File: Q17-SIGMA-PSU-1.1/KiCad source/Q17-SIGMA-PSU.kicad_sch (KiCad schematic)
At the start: 80 parts, among them J1-1 V+ (IN), J1-2 GND, J1-3 V- (IN), J2-1 V+, J2-2 V+, J2-3 GND, J2-4 GND, J2-5 GND, J2-6 V-, J2-7 V-, Q1 BC548B, Q2 BC558B, Q3 BC548B, Q4 BC556B, Q5 BC546B, Q6 IRFZ24NPBF, Q7 IRF9Z34NPBF, Q8 IRFZ24NPBF, Q9 IRF9Z34NPBF, U1 ZHB6792TA, U2 ZHB6792TA

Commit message: Update diagram
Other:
- note added: "Q6, Q8 : IRFZ24NPBF, IRFZ34NPBF or IRF530NPBF"
- note removed: "Q6, Q8 : IRFZ24NPBF or IRF530NPBF"
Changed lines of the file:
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@@
 	(title_block
 		(title "Q17-SIGMA Power Supply")
-		(date "2024-04-30")
-		(rev "1.1.1")
+		(date "2024-05-04")
+		(rev "1.1.2")
 		(company "PCB and BOM by stef")
 		(comment 2 "Design and test by Moor")
@@
 		)
 	)
-	(text "Q6, Q8 : IRFZ24NPBF or IRF530NPBF"
+	(text "Q6, Q8 : IRFZ24NPBF, IRFZ34NPBF or IRF530NPBF"
 		(exclude_from_sim no)
 		(at 14.478 150.622 0)

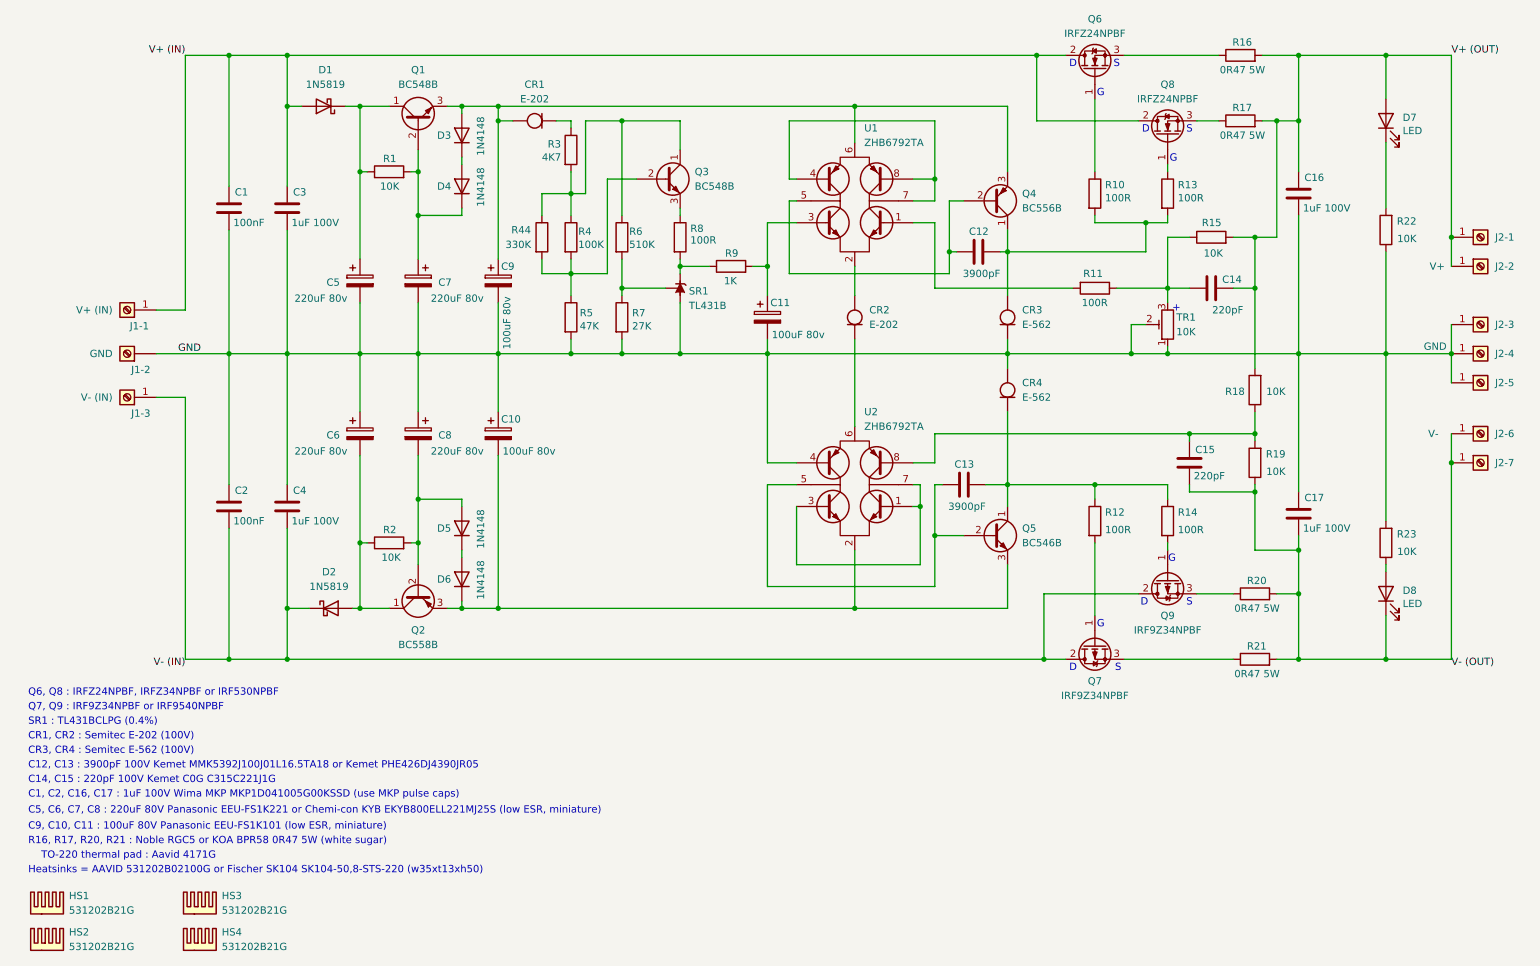
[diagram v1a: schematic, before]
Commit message: Update sigma diagram with real measures
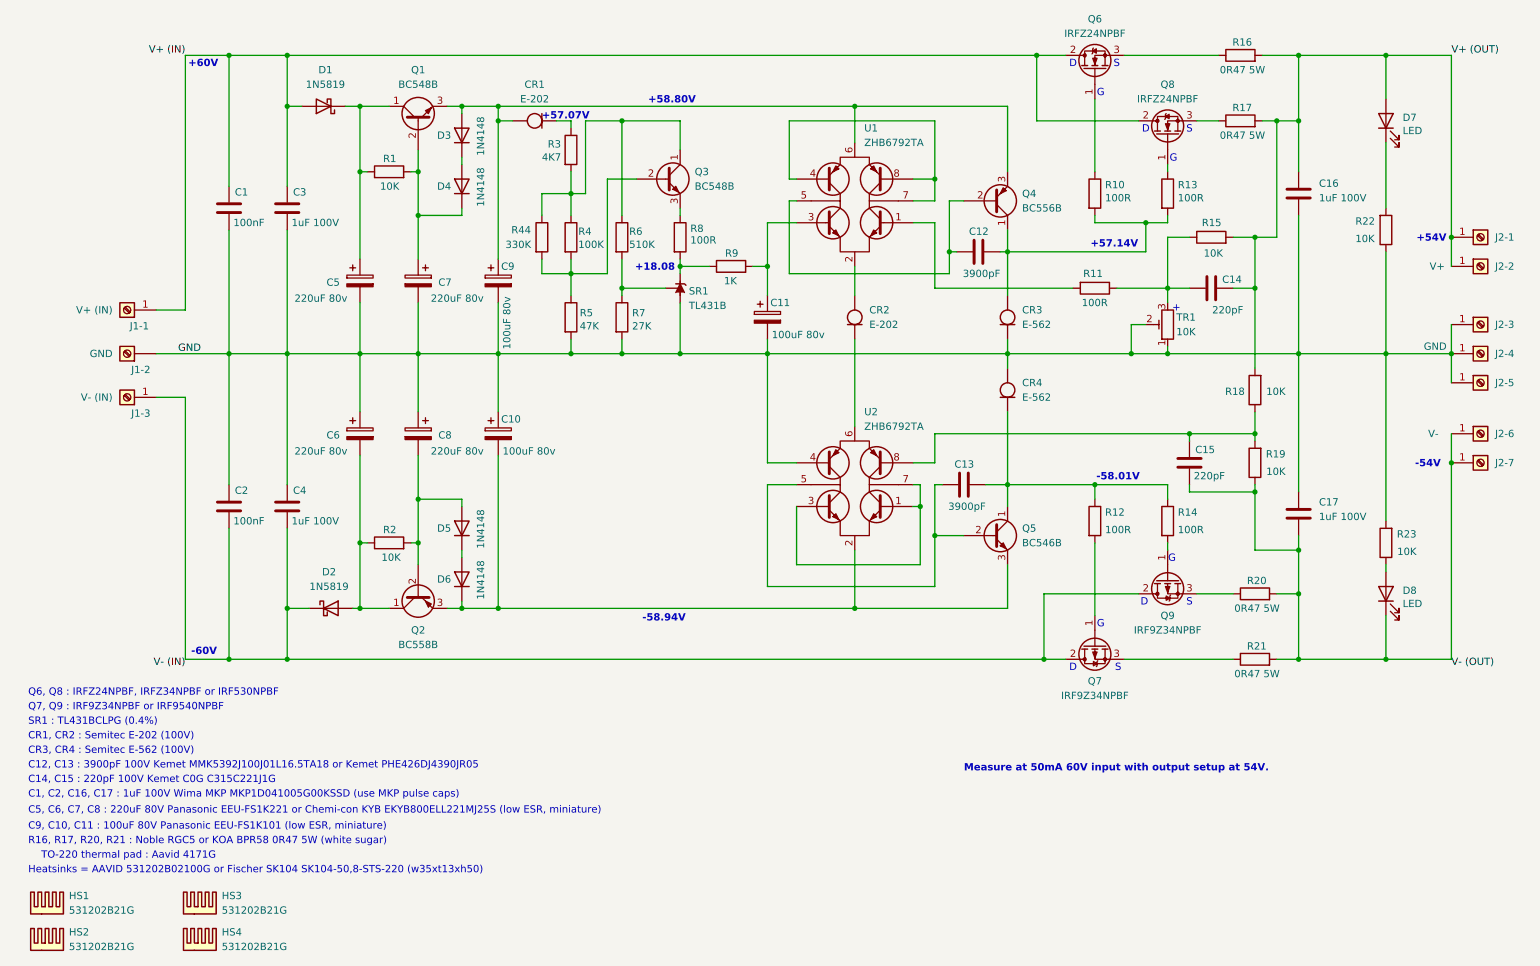
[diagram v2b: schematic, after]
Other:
- note added: "+18.08"
- note added: "+54V"
- note added: "+57.07V"
- note added: "+57.14V"
- note added: "+58.80V"
- note added: "+60V"
- note added: "-54V"
- note added: "-58.01V"
- note added: "-58.94V"
- note added: "-60V"
- note added: "Measure at 50mA 60V input with output setup at 54V."
- moved on the sheet: R22
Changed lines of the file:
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@@
 	(title_block
 		(title "Q17-SIGMA Power Supply")
-		(date "2024-05-04")
-		(rev "1.1.2")
+		(date "2024-05-05")
+		(rev "1.1.3")
 		(company "PCB and BOM by stef")
 		(comment 2 "Design and test by Moor")
@@
 		)
 	)
+	(text "Measure at 50mA 60V input with output setup at 54V."
+		(exclude_from_sim no)
+		(at 177.8 163.83 0)
+		(effects
+			(font
+				(size 1.27 1.27)
+				(thickness 0.254)
+				(bold yes)
+				(color 255 4 17 1)
+			)
+			(justify left)
+		)
+	)
 	(text "C5, C6, C7, C8 : 220uF 80V Panasonic EEU-FS1K221 or Chemi-con KYB EKYB800ELL221MJ25S (low ESR, miniature)"
 		(exclude_from_sim no)
@@
 		)
 	)
+	(text "-58.94V"
+		(exclude_from_sim no)
+		(at 121.666 137.668 0)
+		(effects
+			(font
+				(size 1.27 1.27)
+				(thickness 0.254)
+				(bold yes)
+				(color 255 4 17 1)
+			)
+			(justify left)
+		)
+	)
 	(text "C1, C2, C16, C17 : 1uF 100V Wima MKP MKP1D041005G00KSSD (use MKP pulse caps)"
 		(exclude_from_sim no)
@@
 		)
 	)
+	(text "-54V"
+		(exclude_from_sim no)
+		(at 256.54 110.744 0)
+		(effects
+			(font
+				(size 1.27 1.27)
+				(thickness 0.254)
+				(bold yes)
+				(color 255 4 17 1)
+			)
+			(justify left)
+		)
+	)
 	(text "SR1 : TL431BCLPG (0.4%)"
 		(exclude_from_sim no)
@@
 		)
 	)
+	(text "-58.01V"
+		(exclude_from_sim no)
+		(at 200.914 113.03 0)
+		(effects
+			(font
+				(size 1.27 1.27)
+				(thickness 0.254)
+				(bold yes)
+				(color 255 4 17 1)
+			)
+			(justify left)
+		)
+	)
 	(text "C9, C10, C11 : 100uF 80V Panasonic EEU-FS1K101 (low ESR, miniature)"
 		(exclude_from_sim no)
@@
 		)
 	)
+	(text "+54V"
+		(exclude_from_sim no)
+		(at 256.794 71.374 0)
+		(effects
+			(font
+				(size 1.27 1.27)
+				(thickness 0.254)
+				(bold yes)
+				(color 255 4 17 1)
+			)
+			(justify left)
+		)
+	)
+	(text "+60V"
+		(exclude_from_sim no)
+		(at 42.418 40.894 0)
+		(effects
+			(font
+				(size 1.27 1.27)
+				(thickness 0.254)
+				(bold yes)
+				(color 255 4 17 1)
+			)
+			(justify left)
+		)
+	)
 	(text "G"
 		(exclude_from_sim no)
@@
 		)
 	)
+	(text "+57.14V"
+		(exclude_from_sim no)
+		(at 199.898 72.39 0)
+		(effects
+			(font
+				(size 1.27 1.27)
+				(thickness 0.254)
+				(bold yes)
+				(color 255 4 17 1)
+			)
+			(justify left)
+		)
+	)
+	(text "-60V"
+		(exclude_from_sim no)
+		(at 42.926 143.51 0)
+		(effects
+			(font
+				(size 1.27 1.27)
+				(thickness 0.254)
+				(bold yes)
+				(color 255 4 17 1)
+			)
+			(justify left)
+		)
+	)
 	(text "G"
 		(exclude_from_sim no)
@@
 		)
 	)
+	(text "+58.80V"
+		(exclude_from_sim no)
+		(at 122.682 47.244 0)
+		(effects
+			(font
+				(size 1.27 1.27)
+				(thickness 0.254)
+				(bold yes)
+				(color 255 4 17 1)
+			)
+			(justify left)
+		)
+	)
+	(text "+57.07V"
+		(exclude_from_sim no)
+		(at 104.14 50.038 0)
+		(effects
+			(font
+				(size 1.27 1.27)
+				(thickness 0.254)
+				(bold yes)
+				(color 255 4 17 1)
+			)
+			(justify left)
+		)
+	)
 	(text "S"
 		(exclude_from_sim no)
@@
 		)
 	)
+	(text "+18.08"
+		(exclude_from_sim no)
+		(at 120.396 76.454 0)
+		(effects
+			(font
+				(size 1.27 1.27)
+				(thickness 0.254)
+				(bold yes)
+				(color 255 4 17 1)
+			)
+			(justify left)
+		)
+	)
 	(text "+"
 		(exclude_from_sim no)
@@
 	(symbol
 		(lib_id "Device:R")
-		(at 251.46 69.85 180)
+		(at 251.46 69.85 0)
+		(mirror x)
 		(unit 1)
 		(exclude_from_sim no)
@@
 		(dnp no)
 		(property "Reference" "R22"
-			(at 256.794 68.326 0)
+			(at 246.126 68.326 0)
 			(effects
 				(font
@@
 		)
 		(property "Value" "10K"
-			(at 256.794 71.374 0)
+			(at 246.126 71.374 0)
 			(effects
 				(font
@@
 		)
 		(property "Footprint" "Resistor_THT:R_Axial_DIN0207_L6.3mm_D2.5mm_P10.16mm_Horizontal"
-			(at 253.238 69.85 90)
+			(at 249.682 69.85 90)
 			(effects
 				(font
@@
 		(dnp no)
 		(property "Reference" "C17"
-			(at 237.236 116.586 0)
+			(at 239.776 117.348 0)
 			(effects
 				(font
@@
 		)
 		(property "Value" "1uF 100V"
-			(at 236.982 121.92 0)
+			(at 239.776 119.888 0)
 			(effects
 				(font
@@
 		(dnp no)
 		(property "Reference" "C16"
-			(at 237.236 60.706 0)
+			(at 239.776 61.722 0)
 			(effects
 				(font
@@
 		)
 		(property "Value" "1uF 100V"
-			(at 236.982 66.04 0)
+			(at 239.776 64.262 0)
 			(effects
 				(font
